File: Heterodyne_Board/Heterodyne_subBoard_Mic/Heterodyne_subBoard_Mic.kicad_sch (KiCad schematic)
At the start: 6 parts, among them U2 TLV9054xD

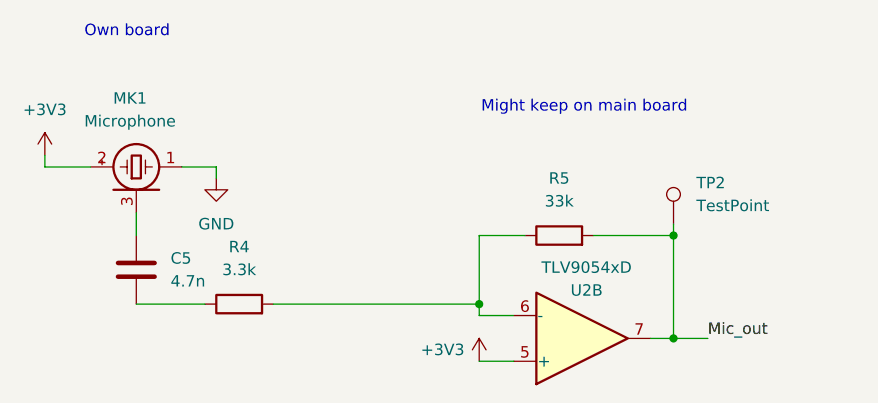
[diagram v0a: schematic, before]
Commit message: Board round 2 complete, GBRs sent
Also removed some of the automatic backups cuz they weren't necessary. Made discrete footprint for microphone
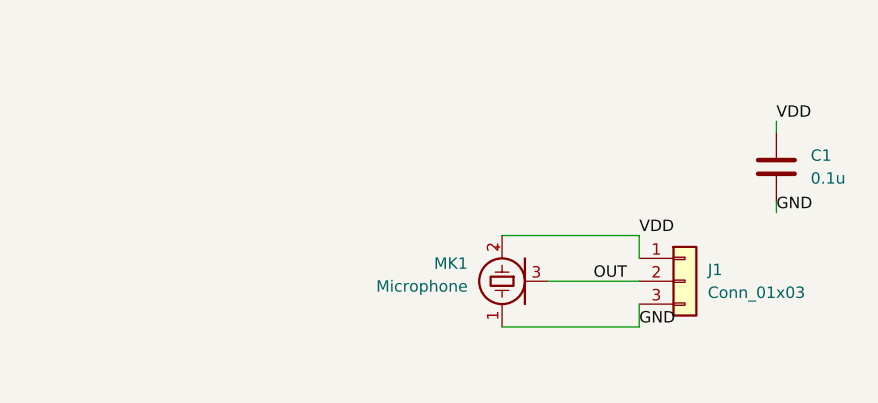
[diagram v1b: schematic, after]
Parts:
- removed C5: 4.7n, Capacitor_SMD:C_0805_2012Metric_Pad1.18x1.45mm_HandSolder, symbol Device:C
- removed R4: 3.3k, Resistor_SMD:R_0805_2012Metric_Pad1.20x1.40mm_HandSolder, symbol Device:R
- removed R5: 33k, Resistor_SMD:R_0805_2012Metric_Pad1.20x1.40mm_HandSolder, symbol Device:R
- removed TP2: TestPoint, TestPoint:TestPoint_Pad_1.0x1.0mm, symbol Connector:TestPoint
- removed U2: TLV9054xD, Package_SO:SOIC-14_3.9x8.7mm_P1.27mm, symbol Amplifier_Operational:TLV9054xD
- added C1: 0.1u, Capacitor_SMD:C_0805_2012Metric_Pad1.18x1.45mm_HandSolder, symbol Device:C
- added J1: Conn_01x03, Connector_PinHeader_2.54mm:PinHeader_1x03_P2.54mm_Vertical, symbol Connector_Generic:Conn_01x03
- MK1: footprint Sensor_Audio:Knowles_LGA-5_3.5x2.65mm -> Mic_Footprint:445_MEMS-5_3.5x2.65mm
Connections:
- net GND: now also C1.2, J1.3 (Pin_3)
- net OUT: now reaches MK1.3 (+)
- net OUT: now also J1.2 (Pin_2)
- net +3V3 renamed VDD
- net VDD: now also C1.1, J1.1 (Pin_1)
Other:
- note removed: "Might keep on main board"
- note removed: "Own board"
- moved on the sheet: MK1
